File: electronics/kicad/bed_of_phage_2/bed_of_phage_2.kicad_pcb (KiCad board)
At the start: 2 copper layers, 12 parts, among them J1 CONN_03, J2 CONN_03, P1 CONN_8, U1 LM358N

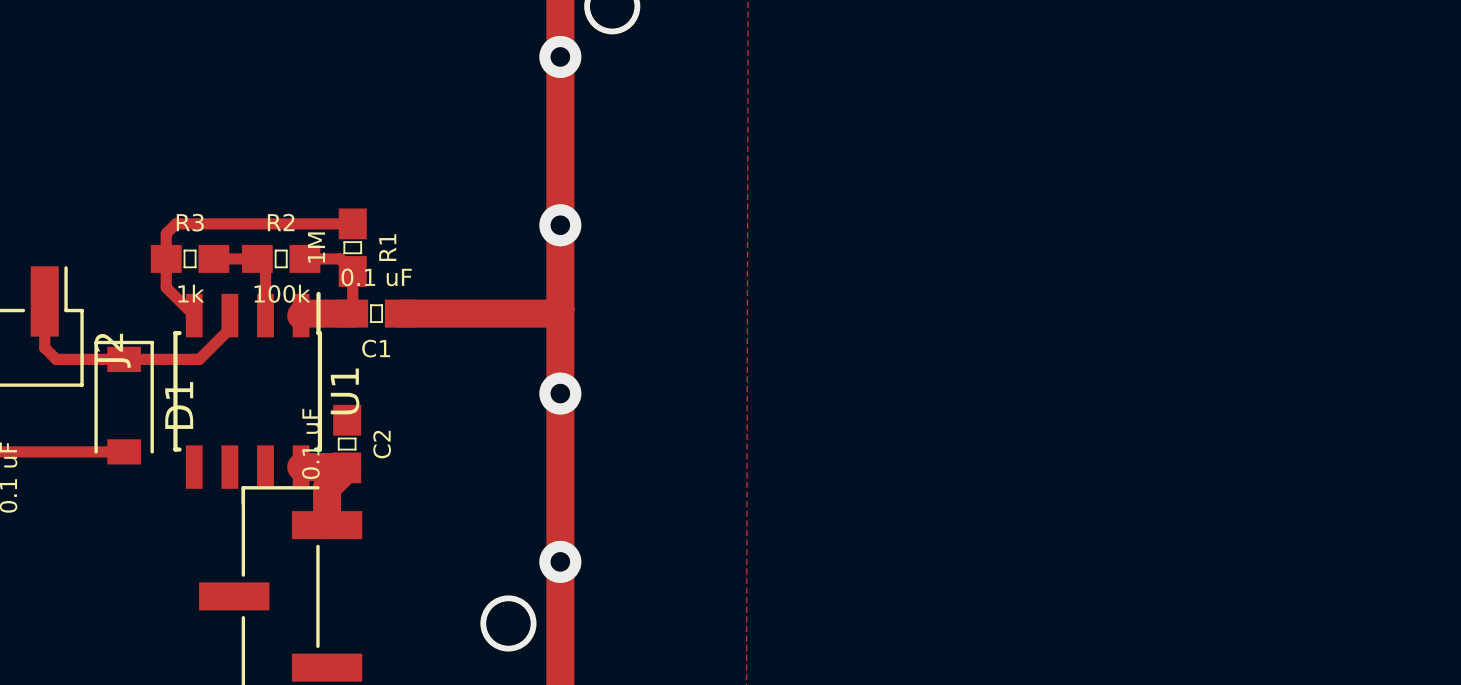
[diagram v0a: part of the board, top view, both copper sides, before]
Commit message: Screwed up a simple op-amp circuit
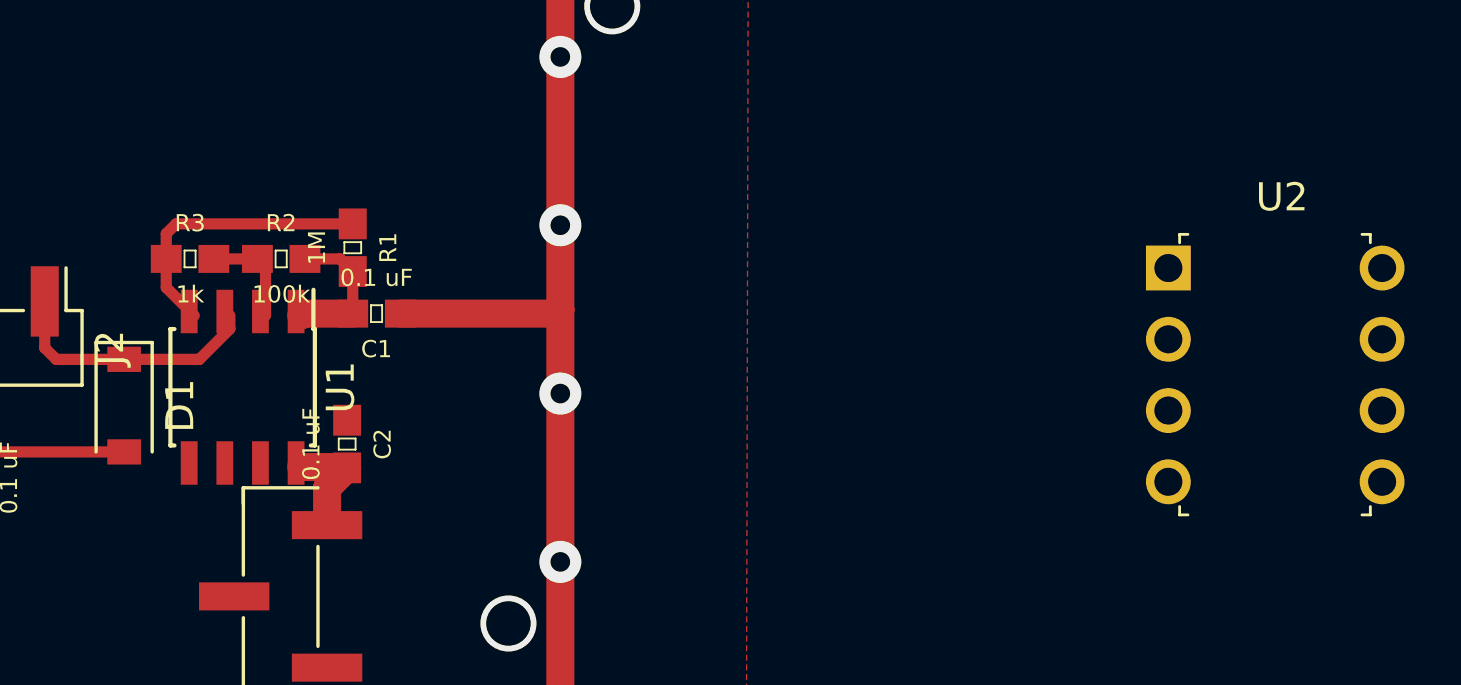
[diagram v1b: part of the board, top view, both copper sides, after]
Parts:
- added U2: LM358N, digikey-footprints:DIP-8_W7.62mm, F.Cu at (120.0, 84.2)
- moved U1 0.23 mm to (87.0, 88.5)
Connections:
- P1 pad 1: (no net) -> /1
- P1 pad 2: (no net) -> /1
- P1 pad 3: (no net) -> /1
- P1 pad 4: (no net) -> /1
- P1 pad 5: (no net) -> /1
- P1 pad 6: (no net) -> /1
- P1 pad 7: (no net) -> /1
- P1 pad 8: (no net) -> /1
- U1 pad 1: Net-(C1-Pad2) -> Net-(D1-Pad1)
- U1 pad 3: Net-(D1-Pad1) -> Net-(C1-Pad2)
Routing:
- net /1: track 0.00 -> 165.5 mm, vias 0 -> 8
- net (no net): track 165.5 -> 0.00 mm, vias 12 -> 4

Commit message: nope, I didn't screw that up.
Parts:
- removed U2: LM358N, digikey-footprints:DIP-8_W7.62mm
- moved C1 6.40 mm to (87.8, 80.9)
- moved C2 6.40 mm to (86.7, 85.5)
- moved C3 6.40 mm to (73.4, 86.7)
- moved D1 6.40 mm to (78.8, 84.2)
- moved J1 6.40 mm to (84.4, 91.0)
- moved J2 6.40 mm to (73.4, 82.1)
- moved R1 6.40 mm to (86.9, 78.5)
- moved R2 6.40 mm to (84.4, 78.9)
- moved R3 6.40 mm to (81.1, 78.9)
- moved R4 6.40 mm to (71.9, 86.7)
- moved U1 6.18 mm to (83.2, 83.6)
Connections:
- P1 pad 1: /1 -> (no net)
- P1 pad 2: /1 -> (no net)
- P1 pad 3: /1 -> (no net)
- P1 pad 4: /1 -> (no net)
- P1 pad 5: /1 -> (no net)
- P1 pad 6: /1 -> (no net)
- P1 pad 7: /1 -> (no net)
- P1 pad 8: /1 -> (no net)
- U1 pad 1: Net-(D1-Pad1) -> Net-(C1-Pad2)
- U1 pad 3: Net-(C1-Pad2) -> Net-(D1-Pad1)
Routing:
- net /1: track 165.5 -> 0.00 mm, vias 8 -> 0
- net (no net): track 0.00 -> 165.5 mm, vias 4 -> 12
- net GND: track 10.9 -> 35.9 mm
